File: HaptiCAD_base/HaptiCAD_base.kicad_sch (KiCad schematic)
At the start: 8 parts, among them J1 EXT_PWR, J2 Encoder, J3 EXT_UART, J4 BLDC

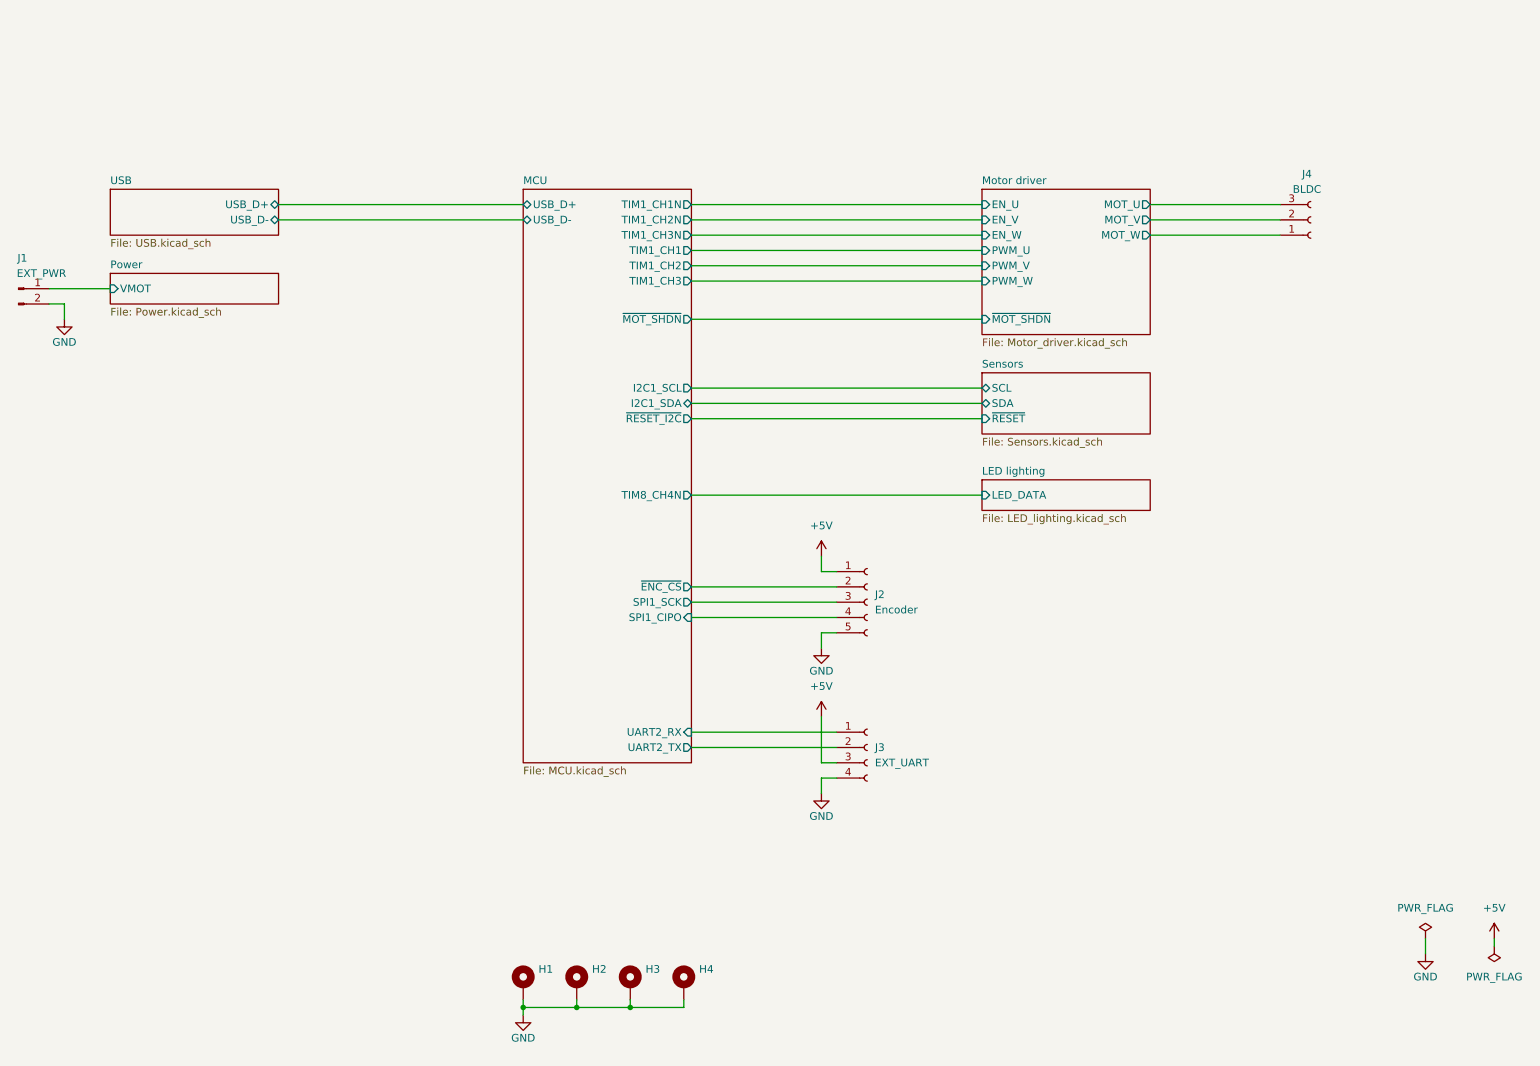
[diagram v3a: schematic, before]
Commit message: Finished the layout for the base and motor mount
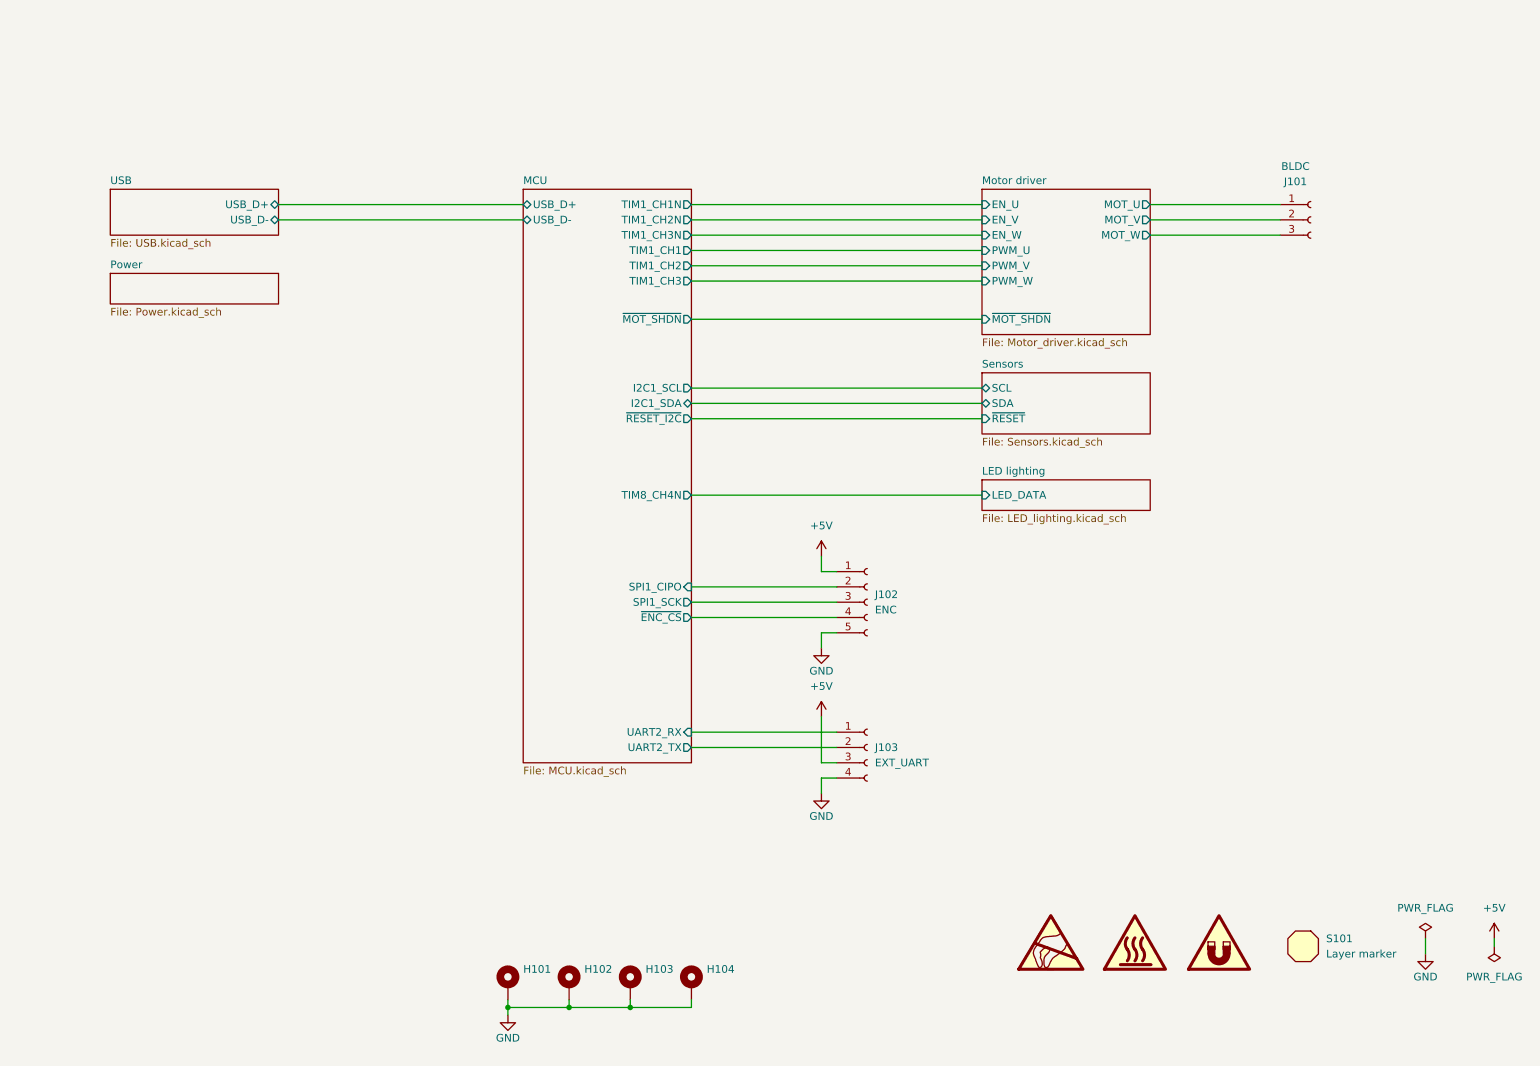
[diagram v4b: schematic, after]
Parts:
- removed J1: EXT_PWR, symbol Connector:Conn_01x02_Pin
- added S101: Layer marker, Symbol:LayerMarker_4_6.35x2.54mm_TextH1mm_P1.27mm_BottomMirrored, symbol Mechanical:Mechanical_Shape
- J101: renamed from J4; footprint Connector_Molex:Molex_SPOX_5267-03A_1x03_P2.50mm_Vertical -> Connector_JST:JST_PH_B3B-PH-SM4-TB_1x03-1MP_P2.00mm_Vertical
- J102: renamed from J2; value Encoder -> ENC; footprint (none) -> Connector_JST:JST_PH_B5B-PH-SM4-TB_1x05-1MP_P2.00mm_Vertical
- J103: renamed from J3; footprint (none) -> Connector_PinHeader_2.54mm:PinHeader_1x04_P2.54mm_Vertical_SMD_Pin1Left
- renumbered H1 to H101, H2 to H102, H3 to H103, H4 to H104
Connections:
- net MCU/SPI1_CIPO: now also J102.2 (Pin_2); no longer J102.4 (Pin_4)
- net MCU/~{ENC_CS}: now also J102.4 (Pin_4); no longer J102.2 (Pin_2)
- net Motor driver/MOT_U: now also J101.1 (Pin_1); no longer J101.3 (Pin_3)
- net Motor driver/MOT_W: now also J101.3 (Pin_3); no longer J101.1 (Pin_1)
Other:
- sheet Power ports: added none; removed VMOT
- moved on the sheet: H101, H102, H104
